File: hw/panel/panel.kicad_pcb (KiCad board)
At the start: 2 copper layers, 100 x 100 mm, 134 parts, among them J1 Barrel_Jack, J2 Conn_ST_STDC14, Q1 BS170F, U1 STM32G031K8Tx, U2 RFM69HW, U3 AMS1117-3.3, U4 MCP16301Hx-xCH, Y1 32.768KHz

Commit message: panel
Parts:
- removed AE1: Antenna, RF_Antenna:NiceRF_SW868-TH13_868Mhz
- removed the C10 at (140.2, 130.0)
- removed the C12 at (98.1, 130.0)
- removed the C13 at (123.4, 130.0)
- removed the C14 at (148.6, 130.0)
- removed the C15 at (81.3, 130.0)
- removed the C16 at (106.5, 130.0)
- removed the C17 at (131.8, 130.0)
- removed the C18 at (157.0, 130.0)
- removed the C21 at (85.0, 139.1)
- removed the C22 at (80.5, 126.0)
- removed the C23 at (74.0, 137.0)
- removed the C7 at (64.5, 130.0)
- removed the D11 at (107.0, 126.8)
- removed the D13 at (141.0, 126.8)
- removed the D15 at (81.4, 126.8)
- removed the D17 at (115.5, 126.8)
- removed the D19 at (149.5, 126.8)
- removed the D21 at (89.9, 126.8)
- removed the D23 at (124.0, 126.8)
- removed the D25 at (158.0, 126.8)
- removed D26: 1N4148W, Diode_SMD:D_SOD-123
- removed D27: B140-E3, Diode_SMD:D_SMA
- removed D29, D31, D33, D35, D37, D39, D41, D43, D45, D47, D49, D51: WS2812B-2020, LED_SMD:LED_WS2812B-2020_PLCC4_2.0x2.0mm
- removed the D3 at (64.4, 126.8)
- removed the D5 at (98.4, 126.8)
- removed the D7 at (132.5, 126.8)
- removed the D9 at (72.9, 126.8)
- removed the JP14 at (125.9, 117.5)
- removed L1: 22uH, Inductor_SMD:L_Coilcraft_LPS4018
- removed R4: 52.3k, Resistor_SMD:R_0805_2012Metric_Pad1.20x1.40mm_HandSolder
- removed R5: 10k, Resistor_SMD:R_0805_2012Metric_Pad1.20x1.40mm_HandSolder
- removed U4: MCP16301Hx-xCH, Package_TO_SOT_SMD:SOT-23-6
- added C26: 100nF, Capacitor_SMD:C_0805_2012Metric_Pad1.18x1.45mm_HandSolder, F.Cu at (112.5, 121.0)
- added C27: 100nF, Capacitor_SMD:C_0805_2012Metric_Pad1.18x1.45mm_HandSolder, F.Cu at (137.5, 121.0)
- added C28: 100nF, Capacitor_SMD:C_0805_2012Metric_Pad1.18x1.45mm_HandSolder, F.Cu at (71.5, 121.0)
- added C29: 100nF, Capacitor_SMD:C_0805_2012Metric_Pad1.18x1.45mm_HandSolder, F.Cu at (96.0, 121.0)
- added C30: 100nF, Capacitor_SMD:C_0805_2012Metric_Pad1.18x1.45mm_HandSolder, F.Cu at (121.0, 121.0)
- added C31: 100nF, Capacitor_SMD:C_0805_2012Metric_Pad1.18x1.45mm_HandSolder, F.Cu at (146.0, 121.0)
- added C32: 100nF, Capacitor_SMD:C_0805_2012Metric_Pad1.18x1.45mm_HandSolder, F.Cu at (79.5, 121.0)
- added C33: 100nF, Capacitor_SMD:C_0805_2012Metric_Pad1.18x1.45mm_HandSolder, F.Cu at (104.5, 121.0)
- added C34: 100nF, Capacitor_SMD:C_0805_2012Metric_Pad1.18x1.45mm_HandSolder, F.Cu at (129.5, 121.0)
- added C35: 100nF, Capacitor_SMD:C_0805_2012Metric_Pad1.18x1.45mm_HandSolder, F.Cu at (154.0, 121.0)
- added J2: Conn_Coaxial, Connector_Coaxial:SMA_Amphenol_901-143_Horizontal, F.Cu at (65.5, 104.0)
- added J4: Conn_01x04_Socket, Connector_PinSocket_2.54mm:PinSocket_1x04_P2.54mm_Horizontal, F.Cu at (159.5, 80.6)
- added J5: Conn_01x04_Pin, Connector_PinHeader_2.54mm:PinHeader_1x04_P2.54mm_Horizontal, F.Cu at (65.5, 80.6)
- C11, C9: moved to B.Cu
- C24, C25: value 10uF -> 100nF; footprint Capacitor_SMD:C_1206_3216Metric_Pad1.33x1.80mm_HandSolder -> Capacitor_SMD:C_0805_2012Metric_Pad1.18x1.45mm_HandSolder; moved to F.Cu
- C8: value 100nF -> 4.7uF; moved to B.Cu
- J1: footprint Connector_BarrelJack:BarrelJack_CUI_PJ-063AH_Horizontal -> Connector_AMASS:AMASS_XT30PW-M_1x02_P2.50mm_Horizontal
- moved JP15 79.7 mm to (156.5, 133.5), turned to 180 degrees
- moved JP16 79.2 mm to (148.2, 133.5), turned to 180 degrees
- moved JP17 79.2 mm to (139.9, 133.5), turned to 180 degrees
- moved JP26 79.2 mm to (65.3, 133.5), turned to 180 degrees
- moved JP18 79.2 mm to (131.6, 133.5), turned to 180 degrees
- moved JP25 79.2 mm to (73.6, 133.5), turned to 180 degrees
- moved JP19 79.2 mm to (123.3, 133.5), turned to 180 degrees
- moved JP24 79.2 mm to (81.9, 133.5), turned to 180 degrees
- moved JP20 79.2 mm to (115.0, 133.5), turned to 180 degrees
- moved JP23 79.2 mm to (90.2, 133.5), turned to 180 degrees
- moved JP21 79.2 mm to (106.7, 133.5), turned to 180 degrees
- moved JP22 79.2 mm to (98.4, 133.5), turned to 180 degrees
- moved D1 76.1 mm to (41.5, 138.5), turned to 90 degrees
- moved R1 72.1 mm to (43.5, 138.5), turned to 90 degrees
- moved D14 67.1 mm to (156.6, 127.0)
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- renumbered C20 to C10, C26 to C12, C30 to C13, C34 to C14, C27 to C15, C31 to C16, C35 to C17, C28 to C18, C32 to C19, C36 to C20, C29 to C21, C33 to C22, C37 to C23, C19 to C7, D6 to D10, D12 to D11, D18 to D12, D24 to D13, D50 to D14, D44 to D15, D38 to D16, D32 to D17, D48 to D18, D42 to D19, D36 to D20, D30 to D21, D46 to D22, D40 to D23, D34 to D24, D28 to D25, D8 to D3, D14 to D4, D20 to D5, D4 to D6, D10 to D7, D16 to D8, D22 to D9, H3 to H2, H2 to H3, J2 to J3, JP2 to JP1, JP9 to JP10, JP5 to JP11, JP10 to JP12, JP6 to JP13, JP11 to JP14, JP25 to JP15, JP22 to JP16, JP19 to JP17, JP16 to JP18, JP24 to JP19, JP26 to JP2, JP21 to JP20, JP18 to JP21, JP15 to JP22, JP20 to JP24, JP17 to JP25, JP14 to JP26, JP1 to JP3, JP7 to JP4, JP12 to JP5, JP3 to JP6, JP8 to JP7, JP13 to JP8, JP4 to JP9, R2 to R1, R1 to R2, U3 to U2, U2 to U3
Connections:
- C11 pad 1: +5V -> +3V3
- C12 pad 1: +5V -> +6V
- C13 pad 1: +5V -> +6V
- C14 pad 1: +5V -> +6V
- C15 pad 1: +5V -> +6V
- C16 pad 1: +5V -> +6V
- C17 pad 1: +5V -> +6V
- C18 pad 1: +5V -> +6V
- C19 pad 1: +5V -> +6V
- C20 pad 1: +5V -> +6V
- C21 pad 1: +5V -> +6V
- C22 pad 1: +5V -> +6V
- C23 pad 1: +5V -> +6V
- C24 pad 1: +5V -> +6V
- C25 pad 1: Net-(U4-EN) -> +6V
- C7 pad 1: +5V -> +6V
- C8 pad 1: +5V -> +3V3
- C9 pad 1: +5V -> +3V3
- D10 pad 1: +5V -> +6V
- D10 pad 2: Net-(D6-DOUT) -> Net-(D10-DOUT)
- D10 pad 4: Net-(D4-DOUT) -> Net-(D10-DIN)
- D11 pad 1: +5V -> +6V
- D11 pad 2: Net-(D12-DOUT) -> Net-(D11-DOUT)
- D12 pad 1: +5V -> +6V
- D12 pad 2: Net-(D18-DOUT) -> Net-(D12-DOUT)
- D12 pad 4: Net-(D16-DOUT) -> Net-(D11-DOUT)
- D13 pad 1: +5V -> +6V
- D13 pad 4: Net-(D22-DOUT) -> Net-(D12-DOUT)
- D14 pad 1: +5V -> +6V
- D14 pad 2: /leds1/RGB_OUT -> Net-(D14-DOUT)
- D14 pad 4: Net-(D48-DOUT) -> /leds1/RGB_IN
- D15 pad 1: +5V -> +6V
- D15 pad 2: Net-(D44-DOUT) -> Net-(D15-DOUT)
- D15 pad 4: Net-(D42-DOUT) -> Net-(D14-DOUT)
- D16 pad 1: +5V -> +6V
- D16 pad 2: Net-(D38-DOUT) -> Net-(D16-DOUT)
- D16 pad 4: Net-(D36-DOUT) -> Net-(D15-DOUT)
- D17 pad 1: +5V -> +6V
- D17 pad 2: Net-(D32-DOUT) -> Net-(D17-DOUT)
- D17 pad 4: Net-(D30-DOUT) -> Net-(D16-DOUT)
- D18 pad 1: +5V -> +6V
- D18 pad 2: Net-(D48-DOUT) -> Net-(D18-DOUT)
- D18 pad 4: Net-(D46-DOUT) -> Net-(D17-DOUT)
- D19 pad 1: +5V -> +6V
- D19 pad 2: Net-(D42-DOUT) -> Net-(D19-DOUT)
- D19 pad 4: Net-(D40-DOUT) -> Net-(D18-DOUT)
- D2 pad 1: +5V -> +6V
- D20 pad 1: +5V -> +6V
- D20 pad 2: Net-(D36-DOUT) -> Net-(D20-DOUT)
- D20 pad 4: Net-(D34-DOUT) -> Net-(D19-DOUT)
- D21 pad 1: +5V -> +6V
- D21 pad 2: Net-(D30-DOUT) -> Net-(D21-DOUT)
- D21 pad 4: Net-(D28-DOUT) -> Net-(D20-DOUT)
- D22 pad 1: +5V -> +6V
- D22 pad 2: Net-(D46-DOUT) -> Net-(D22-DOUT)
- D22 pad 4: Net-(D44-DOUT) -> Net-(D21-DOUT)
- D23 pad 1: +5V -> +6V
- D23 pad 2: Net-(D40-DOUT) -> Net-(D23-DOUT)
- D23 pad 4: Net-(D38-DOUT) -> Net-(D22-DOUT)
- D24 pad 1: +5V -> +6V
- D24 pad 2: Net-(D34-DOUT) -> Net-(D24-DOUT)
- D24 pad 4: Net-(D32-DOUT) -> Net-(D23-DOUT)
- D25 pad 1: +5V -> +6V
- D25 pad 2: Net-(D28-DOUT) -> /leds1/RGB_OUT
- D25 pad 4: /leds1/RGB_IN -> Net-(D24-DOUT)
- D3 pad 1: +5V -> +6V
- D3 pad 2: Net-(D10-DIN) -> Net-(D3-DOUT)
- D3 pad 4: Net-(D6-DOUT) -> Net-(D2-DOUT)
- D4 pad 1: +5V -> +6V
- D4 pad 2: Net-(D14-DOUT) -> Net-(D4-DOUT)
- D4 pad 4: Net-(D12-DOUT) -> Net-(D3-DOUT)
- D5 pad 1: +5V -> +6V
- D5 pad 2: Net-(D20-DOUT) -> Net-(D5-DOUT)
- D5 pad 4: Net-(D18-DOUT) -> Net-(D4-DOUT)
- D6 pad 1: +5V -> +6V
- D6 pad 2: Net-(D4-DOUT) -> Net-(D6-DOUT)
- D6 pad 4: Net-(D2-DOUT) -> Net-(D5-DOUT)
- D7 pad 1: +5V -> +6V
- D7 pad 2: Net-(D10-DOUT) -> Net-(D7-DOUT)
- D7 pad 4: Net-(D10-DIN) -> Net-(D6-DOUT)
- D8 pad 1: +5V -> +6V
- D8 pad 2: Net-(D16-DOUT) -> Net-(D8-DOUT)
- D8 pad 4: Net-(D14-DOUT) -> Net-(D7-DOUT)
- D9 pad 1: +5V -> +6V
- D9 pad 2: Net-(D22-DOUT) -> Net-(D10-DIN)
- D9 pad 4: Net-(D20-DOUT) -> Net-(D8-DOUT)
- J1 pad 1: Net-(U4-EN) -> +6V
- JP10 pad 1: Net-(D14-DOUT) -> Net-(D8-DOUT)
- JP10 pad 2: Net-(D16-DOUT) -> Net-(D10-DIN)
- JP11 pad 1: Net-(D6-DOUT) -> Net-(D10-DIN)
- JP11 pad 2: Net-(D10-DIN) -> Net-(D10-DOUT)
- JP12 pad 1: Net-(D16-DOUT) -> Net-(D10-DOUT)
- JP12 pad 2: Net-(D18-DOUT) -> Net-(D11-DOUT)
- JP13 pad 1: Net-(D10-DIN) -> Net-(D11-DOUT)
- JP13 pad 2: Net-(D10-DOUT) -> Net-(D12-DOUT)
- JP14 pad 1: Net-(D18-DOUT) -> Net-(D12-DOUT)
- JP14 pad 2: Net-(D20-DOUT) -> /leds/RGB_OUT
- JP15 pad 1: Net-(D48-DOUT) -> /leds1/RGB_IN
- JP15 pad 2: /leds1/RGB_OUT -> Net-(D14-DOUT)
- JP16 pad 1: Net-(D42-DOUT) -> Net-(D14-DOUT)
- JP16 pad 2: Net-(D44-DOUT) -> Net-(D15-DOUT)
- JP17 pad 1: Net-(D36-DOUT) -> Net-(D15-DOUT)
- JP17 pad 2: Net-(D38-DOUT) -> Net-(D16-DOUT)
- JP18 pad 1: Net-(D30-DOUT) -> Net-(D16-DOUT)
- JP18 pad 2: Net-(D32-DOUT) -> Net-(D17-DOUT)
- JP19 pad 1: Net-(D46-DOUT) -> Net-(D17-DOUT)
- JP19 pad 2: Net-(D48-DOUT) -> Net-(D18-DOUT)
- JP20 pad 1: Net-(D40-DOUT) -> Net-(D18-DOUT)
- JP20 pad 2: Net-(D42-DOUT) -> Net-(D19-DOUT)
- JP21 pad 1: Net-(D34-DOUT) -> Net-(D19-DOUT)
- JP21 pad 2: Net-(D36-DOUT) -> Net-(D20-DOUT)
- JP22 pad 1: Net-(D28-DOUT) -> Net-(D20-DOUT)
- JP22 pad 2: Net-(D30-DOUT) -> Net-(D21-DOUT)
- JP23 pad 1: Net-(D44-DOUT) -> Net-(D21-DOUT)
- JP23 pad 2: Net-(D46-DOUT) -> Net-(D22-DOUT)
- JP24 pad 1: Net-(D38-DOUT) -> Net-(D22-DOUT)
- JP24 pad 2: Net-(D40-DOUT) -> Net-(D23-DOUT)
- JP25 pad 1: Net-(D32-DOUT) -> Net-(D23-DOUT)
- JP25 pad 2: Net-(D34-DOUT) -> Net-(D24-DOUT)
- JP26 pad 1: /leds1/RGB_IN -> Net-(D24-DOUT)
- JP26 pad 2: Net-(D28-DOUT) -> /leds1/RGB_OUT
- JP4 pad 1: Net-(D10-DOUT) -> Net-(D2-DOUT)
- JP4 pad 2: Net-(D12-DOUT) -> Net-(D3-DOUT)
- JP5 pad 1: Net-(D20-DOUT) -> Net-(D3-DOUT)
- JP5 pad 2: Net-(D22-DOUT) -> Net-(D4-DOUT)
- JP6 pad 1: Net-(D2-DOUT) -> Net-(D4-DOUT)
- JP6 pad 2: Net-(D4-DOUT) -> Net-(D5-DOUT)
- JP7 pad 1: Net-(D12-DOUT) -> Net-(D5-DOUT)
- JP7 pad 2: Net-(D14-DOUT) -> Net-(D6-DOUT)
- JP8 pad 1: Net-(D22-DOUT) -> Net-(D6-DOUT)
- JP8 pad 2: /leds/RGB_OUT -> Net-(D7-DOUT)
- JP9 pad 1: Net-(D4-DOUT) -> Net-(D7-DOUT)
- JP9 pad 2: Net-(D6-DOUT) -> Net-(D8-DOUT)
- R3 pad 1: +5V -> +6V
- U2 pad 3: +5V -> +6V
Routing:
- net +6V: track 0.00 -> 257.2 mm
- net /RFM_IRQ: track 94.0 -> 15.5 mm, vias 2 -> 0
- net /RFM_SCK: track 104.0 -> 33.1 mm
- net /leds1/RGB_OUT: track 0.00 -> 69.3 mm
- net /RFM_RESET: track 89.0 -> 20.2 mm, vias 0 -> 2
- net /RFM_MOSI: track 99.5 -> 34.1 mm
- net /RFM_MISO: track 96.4 -> 33.6 mm, vias 2 -> 0
- net /leds1/RGB_IN: track 0.00 -> 52.7 mm
- net /RFM_CS: track 93.4 -> 40.8 mm
- net /leds/RGB_IN: track 0.00 -> 50.1 mm
- net +5V: track 35.7 -> 0.00 mm
- net /leds/RGB_OUT: track 0.00 -> 28.8 mm
- net Net-(Q1-S): track 0.00 -> 28.3 mm, vias 0 -> 2
- net /UART_TX: track 22.5 -> 0.00 mm
- net /UART_RX: track 20.1 -> 0.00 mm
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- added copper zone on B.Cu, net GND
- added copper zone on F.Cu, net GND
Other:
- board text added: "win panel v1"

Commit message: panel progress
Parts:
- D1: moved to F.Cu
- J1: footprint Connector_AMASS:AMASS_XT30PW-M_1x02_P2.50mm_Horizontal -> Connector_Molex:Molex_Micro-Fit_3.0_43650-0200_1x02_P3.00mm_Horizontal
- J2, J4, J5: moved to B.Cu
- moved D1 29.5 mm to (71.0, 139.1)
- moved R1 29.5 mm to (73.0, 139.1)
- moved C10 24.8 mm to (101.5, 101.5), turned to 180 degrees
- moved U2 21.9 mm to (103.0, 107.6)
- moved J1 20.3 mm to (80.5, 135.2)
- moved J3 19.8 mm to (92.2, 137.3)
- moved C7 19.1 mm to (103.0, 114.5), turned to 0 degrees
- moved C1 10.8 mm to (103.4, 82.7)
- moved C3 10.8 mm to (105.4, 82.7)
- moved C5 10.8 mm to (108.3, 82.0)
- moved U1 10.8 mm to (106.7, 92.5)
- moved Y1 10.8 mm to (104.2, 86.1)
- moved C2 10.8 mm to (108.3, 86.0)
- moved C4 10.8 mm to (108.3, 84.0)
- moved C6 10.8 mm to (112.8, 87.8)
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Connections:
- D1 pad 2: Net-(D1-A) -> +3V3
- R1 pad 1: +3V3 -> Net-(D1-K)
- R1 pad 2: Net-(D1-A) -> Net-(U1-PC6)
- U1 pad 20: Net-(D1-K) -> Net-(U1-PC6)
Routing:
- net +6V: track 257.2 -> 386.4 mm, vias 0 -> 4
- net +3V3: track 14.1 -> 105.5 mm, vias 0 -> 2
- net Net-(U1-PC6): track 0.00 -> 75.6 mm
- net /RST: track 4.90 -> 65.8 mm, vias 0 -> 1
- net /UART_RX: track 0.00 -> 56.7 mm, vias 0 -> 3
- net /SWDIO: track 0.00 -> 54.5 mm
- net /UART_TX: track 0.00 -> 54.3 mm, vias 0 -> 2
- net /SWCLK: track 0.00 -> 54.0 mm
- net /leds/RGB_IN: track 50.1 -> 61.8 mm
- net Net-(D24-DOUT): track 4.74 -> 15.2 mm
- net Net-(D23-DOUT): track 4.74 -> 15.2 mm
- net Net-(D22-DOUT): track 4.74 -> 15.2 mm
- net Net-(D21-DOUT): track 4.74 -> 15.1 mm
- net Net-(D20-DOUT): track 4.74 -> 15.1 mm
- net Net-(D19-DOUT): track 4.74 -> 15.1 mm
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
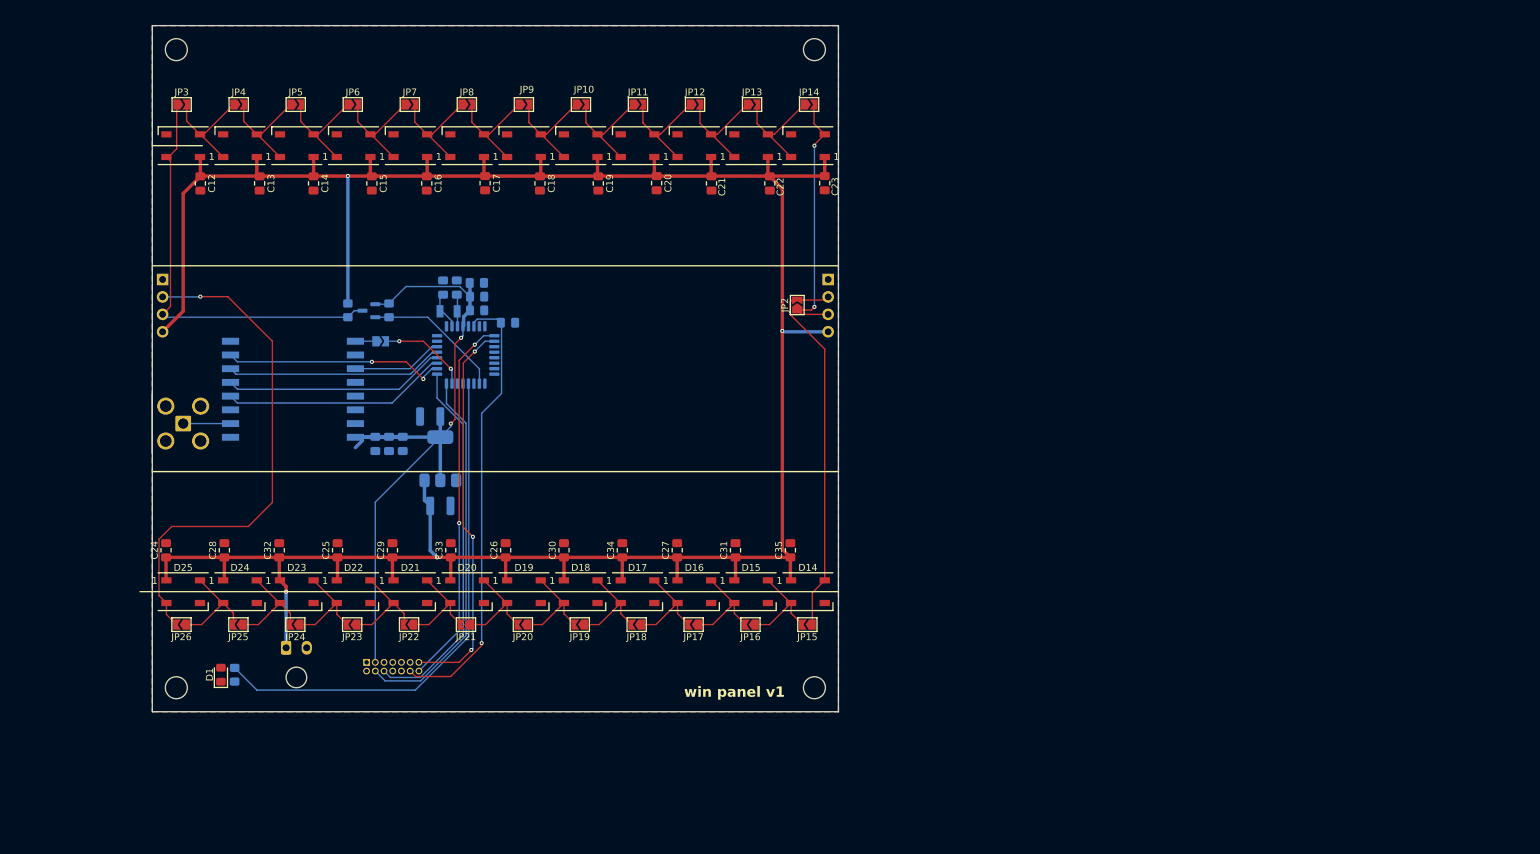
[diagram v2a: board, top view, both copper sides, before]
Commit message: extend top to 200mm
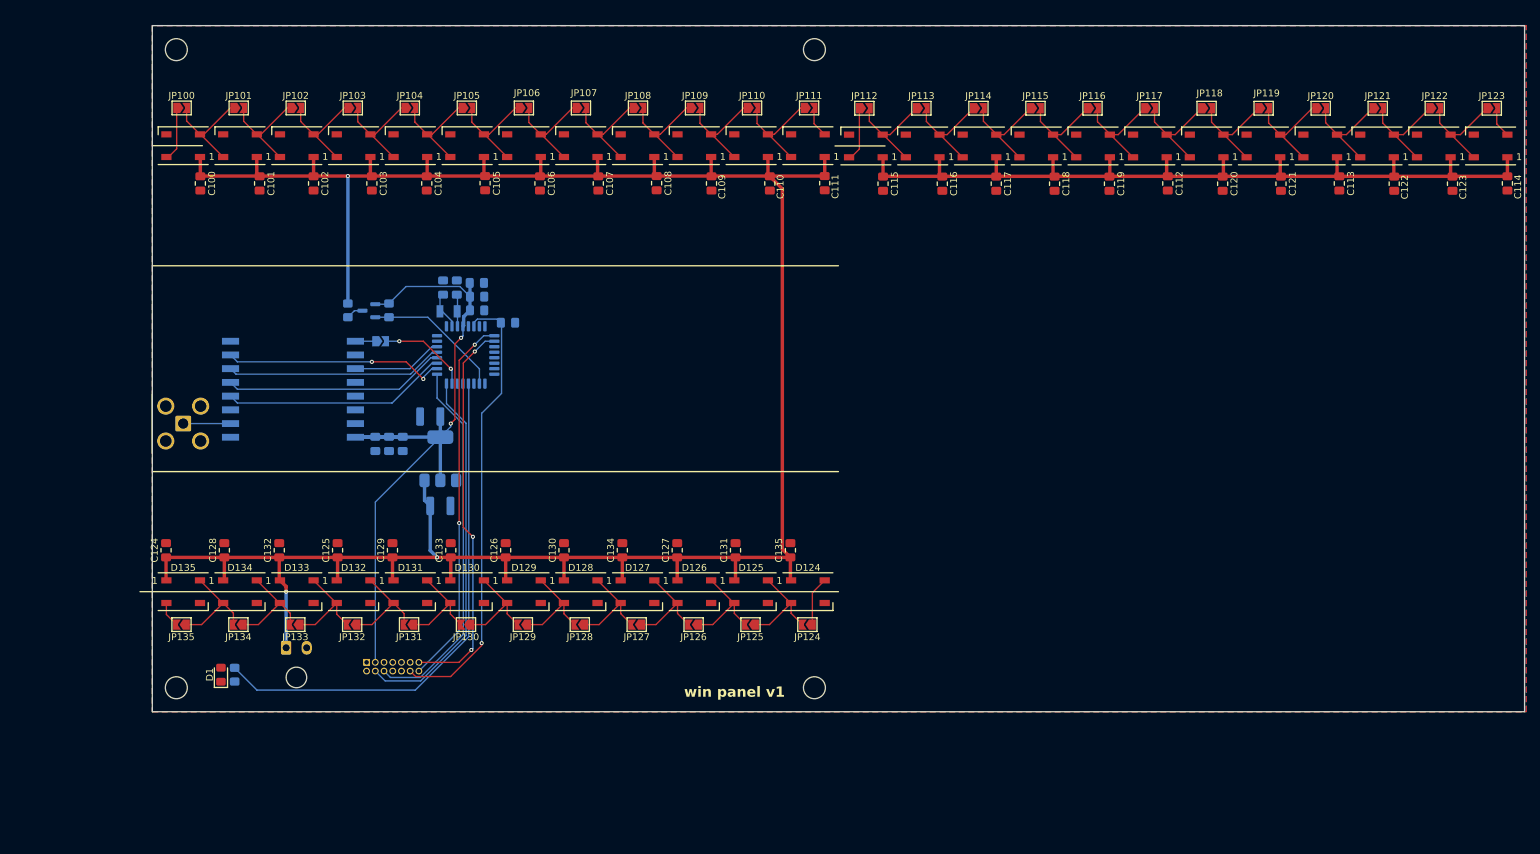
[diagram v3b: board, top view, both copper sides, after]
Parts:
- removed J4: Conn_01x04_Socket, Connector_PinSocket_2.54mm:PinSocket_1x04_P2.54mm_Horizontal
- removed J5: Conn_01x04_Pin, Connector_PinHeader_2.54mm:PinHeader_1x04_P2.54mm_Horizontal
- removed JP2: SolderJumper_2_Bridged, Jumper:SolderJumper-2_P1.3mm_Open_TrianglePad1.0x1.5mm
- added C112: 100nF, Capacitor_SMD:C_0805_2012Metric_Pad1.18x1.45mm_HandSolder, F.Cu at (209.0, 67.5)
- added C113: 100nF, Capacitor_SMD:C_0805_2012Metric_Pad1.18x1.45mm_HandSolder, F.Cu at (234.0, 67.5)
- added C114: 100nF, Capacitor_SMD:C_0805_2012Metric_Pad1.18x1.45mm_HandSolder, F.Cu at (258.5, 67.5)
- added C115: 100nF, Capacitor_SMD:C_0805_2012Metric_Pad1.18x1.45mm_HandSolder, F.Cu at (167.5, 67.5)
- added C116: 100nF, Capacitor_SMD:C_0805_2012Metric_Pad1.18x1.45mm_HandSolder, F.Cu at (176.1, 67.5)
- added C117: 100nF, Capacitor_SMD:C_0805_2012Metric_Pad1.18x1.45mm_HandSolder, F.Cu at (184.0, 67.5)
- added C118: 100nF, Capacitor_SMD:C_0805_2012Metric_Pad1.18x1.45mm_HandSolder, F.Cu at (192.5, 67.5)
- added C119: 100nF, Capacitor_SMD:C_0805_2012Metric_Pad1.18x1.45mm_HandSolder, F.Cu at (200.5, 67.5)
- added C120: 100nF, Capacitor_SMD:C_0805_2012Metric_Pad1.18x1.45mm_HandSolder, F.Cu at (217.0, 67.5)
- added C121: 100nF, Capacitor_SMD:C_0805_2012Metric_Pad1.18x1.45mm_HandSolder, F.Cu at (225.5, 67.5)
- added C122: 100nF, Capacitor_SMD:C_0805_2012Metric_Pad1.18x1.45mm_HandSolder, F.Cu at (242.0, 67.5)
- added C123: 100nF, Capacitor_SMD:C_0805_2012Metric_Pad1.18x1.45mm_HandSolder, F.Cu at (250.5, 67.5)
- added D112: WS2812B, LED_SMD:LED_WS2812B_PLCC4_5.0x5.0mm_P3.2mm, F.Cu at (165.0, 62.0)
- added D113: WS2812B, LED_SMD:LED_WS2812B_PLCC4_5.0x5.0mm_P3.2mm, F.Cu at (173.3, 62.0)
- added D114: WS2812B, LED_SMD:LED_WS2812B_PLCC4_5.0x5.0mm_P3.2mm, F.Cu at (181.6, 62.0)
- added D115: WS2812B, LED_SMD:LED_WS2812B_PLCC4_5.0x5.0mm_P3.2mm, F.Cu at (189.8, 62.0)
- added D116: WS2812B, LED_SMD:LED_WS2812B_PLCC4_5.0x5.0mm_P3.2mm, F.Cu at (198.1, 62.0)
- added D117: WS2812B, LED_SMD:LED_WS2812B_PLCC4_5.0x5.0mm_P3.2mm, F.Cu at (206.4, 62.0)
- added D118: WS2812B, LED_SMD:LED_WS2812B_PLCC4_5.0x5.0mm_P3.2mm, F.Cu at (214.7, 62.0)
- added D119: WS2812B, LED_SMD:LED_WS2812B_PLCC4_5.0x5.0mm_P3.2mm, F.Cu at (222.9, 62.0)
- added D120: WS2812B, LED_SMD:LED_WS2812B_PLCC4_5.0x5.0mm_P3.2mm, F.Cu at (231.2, 62.0)
- added D121: WS2812B, LED_SMD:LED_WS2812B_PLCC4_5.0x5.0mm_P3.2mm, F.Cu at (239.5, 62.0)
- added D122: WS2812B, LED_SMD:LED_WS2812B_PLCC4_5.0x5.0mm_P3.2mm, F.Cu at (247.8, 62.0)
- added D123: WS2812B, LED_SMD:LED_WS2812B_PLCC4_5.0x5.0mm_P3.2mm, F.Cu at (256.1, 62.0)
- added JP112: SolderJumper_2_Open, Jumper:SolderJumper-2_P1.3mm_Open_TrianglePad1.0x1.5mm, F.Cu at (164.8, 56.5)
- added JP113: SolderJumper_2_Open, Jumper:SolderJumper-2_P1.3mm_Open_TrianglePad1.0x1.5mm, F.Cu at (173.1, 56.5)
- added JP114: SolderJumper_2_Open, Jumper:SolderJumper-2_P1.3mm_Open_TrianglePad1.0x1.5mm, F.Cu at (181.4, 56.5)
- added JP115: SolderJumper_2_Open, Jumper:SolderJumper-2_P1.3mm_Open_TrianglePad1.0x1.5mm, F.Cu at (189.7, 56.5)
- added JP116: SolderJumper_2_Open, Jumper:SolderJumper-2_P1.3mm_Open_TrianglePad1.0x1.5mm, F.Cu at (198.0, 56.5)
- added JP117: SolderJumper_2_Open, Jumper:SolderJumper-2_P1.3mm_Open_TrianglePad1.0x1.5mm, F.Cu at (206.3, 56.5)
- added JP118: SolderJumper_2_Open, Jumper:SolderJumper-2_P1.3mm_Open_TrianglePad1.0x1.5mm, F.Cu at (214.7, 56.5)
- added JP119: SolderJumper_2_Open, Jumper:SolderJumper-2_P1.3mm_Open_TrianglePad1.0x1.5mm, F.Cu at (223.0, 56.5)
- added JP120: SolderJumper_2_Open, Jumper:SolderJumper-2_P1.3mm_Open_TrianglePad1.0x1.5mm, F.Cu at (231.3, 56.5)
- added JP121: SolderJumper_2_Open, Jumper:SolderJumper-2_P1.3mm_Open_TrianglePad1.0x1.5mm, F.Cu at (239.6, 56.5)
- added JP122: SolderJumper_2_Open, Jumper:SolderJumper-2_P1.3mm_Open_TrianglePad1.0x1.5mm, F.Cu at (247.9, 56.5)
- added JP123: SolderJumper_2_Open, Jumper:SolderJumper-2_P1.3mm_Open_TrianglePad1.0x1.5mm, F.Cu at (256.2, 56.5)
- moved JP100 0.50 mm to (65.3, 56.5)
- moved JP101 0.50 mm to (73.6, 56.5)
- moved JP102 0.50 mm to (81.9, 56.5)
- moved JP103 0.50 mm to (90.2, 56.5)
- moved JP104 0.50 mm to (98.5, 56.5)
- moved JP105 0.50 mm to (106.8, 56.5)
- moved JP106 0.50 mm to (115.2, 56.5)
- moved JP107 0.50 mm to (123.5, 56.5)
- moved JP108 0.50 mm to (131.8, 56.5)
- moved JP109 0.50 mm to (140.1, 56.5)
- moved JP110 0.50 mm to (148.4, 56.5)
- moved JP111 0.50 mm to (156.7, 56.5)
- renumbered C12 to C100, C13 to C101, C14 to C102, C15 to C103, C16 to C104, C17 to C105, C18 to C106, C19 to C107, C20 to C108, C21 to C109, C22 to C110, C23 to C111, C24 to C124, C25 to C125, C26 to C126, C27 to C127, C28 to C128, C29 to C129, C30 to C130, C31 to C131, C32 to C132, C33 to C133, C34 to C134, C35 to C135, D2 to D100, D3 to D101, D4 to D102, D5 to D103, D6 to D104, D7 to D105, D8 to D106, D9 to D107, D10 to D108, D11 to D109, D12 to D110, D13 to D111, D14 to D124, D15 to D125, D16 to D126, D17 to D127, D18 to D128, D19 to D129, D20 to D130, D21 to D131, D22 to D132, D23 to D133, D24 to D134, D25 to D135, JP3 to JP100, JP4 to JP101, JP5 to JP102, JP6 to JP103, JP7 to JP104, JP8 to JP105, JP9 to JP106, JP10 to JP107, JP11 to JP108, JP12 to JP109, JP13 to JP110, JP14 to JP111, JP15 to JP124, JP16 to JP125, JP17 to JP126, JP18 to JP127, JP19 to JP128, JP20 to JP129, JP21 to JP130, JP22 to JP131, JP23 to JP132, JP24 to JP133, JP25 to JP134, JP26 to JP135
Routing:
- net +6V: track 386.4 -> 480.1 mm, vias 4 -> 3
- net /leds1/RGB_OUT: track 74.5 -> 3.76 mm, vias 1 -> 0
- net /leds/RGB_IN: track 61.8 -> 11.0 mm
- net /leds1/RGB_IN: track 55.7 -> 7.20 mm
- net /leds/RGB_OUT: track 38.2 -> 13.4 mm, vias 2 -> 0
- net Net-(D119-DOUT): track 0.00 -> 16.8 mm
- net Net-(D122-DOUT): track 0.00 -> 16.1 mm
- net Net-(D121-DOUT): track 0.00 -> 16.1 mm
- net Net-(D120-DOUT): track 0.00 -> 16.0 mm
- net Net-(D118-DOUT): track 0.00 -> 16.0 mm
- net Net-(D117-DOUT): track 0.00 -> 16.0 mm
- net Net-(D116-DOUT): track 0.00 -> 16.0 mm
- net Net-(D113-DOUT): track 0.00 -> 15.9 mm
- net Net-(D115-DOUT): track 0.00 -> 15.9 mm
- net Net-(D112-DOUT): track 0.00 -> 15.9 mm
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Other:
- board size 100 x 100 mm -> 200 x 100 mm

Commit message: bot left
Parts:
- renumbered C124 to C212, C125 to C213, C126 to C214, C127 to C215, C128 to C216, C129 to C217, C130 to C218, C131 to C219, C132 to C220, C133 to C221, C134 to C222, C135 to C223, D124 to D212, D125 to D213, D126 to D214, D127 to D215, D128 to D216, D129 to D217, D130 to D218, D131 to D219, D132 to D220, D133 to D221, D134 to D222, D135 to D223, JP124 to JP212, JP125 to JP213, JP126 to JP214, JP127 to JP215, JP128 to JP216, JP129 to JP217, JP130 to JP218, JP131 to JP219, JP132 to JP220, JP133 to JP221, JP134 to JP222, JP135 to JP223
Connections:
- net /leds/RGB_IN renamed /led_top_left/RGB_IN
- net /leds/RGB_OUT renamed /led_top_left/RGB_OUT
- net /leds1/RGB_IN renamed /led_bot_left/RGB_IN
- net /leds1/RGB_OUT renamed /led_bot_left/RGB_OUT
- net /leds2/RGB_OUT renamed /led_top_right/RGB_OUT
